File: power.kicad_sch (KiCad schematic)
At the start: 22 parts, among them J5 Power In, Q1 Q_NMOS_GDS, U5 UMW_HT7533-1_3.3V_High-In_LDO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

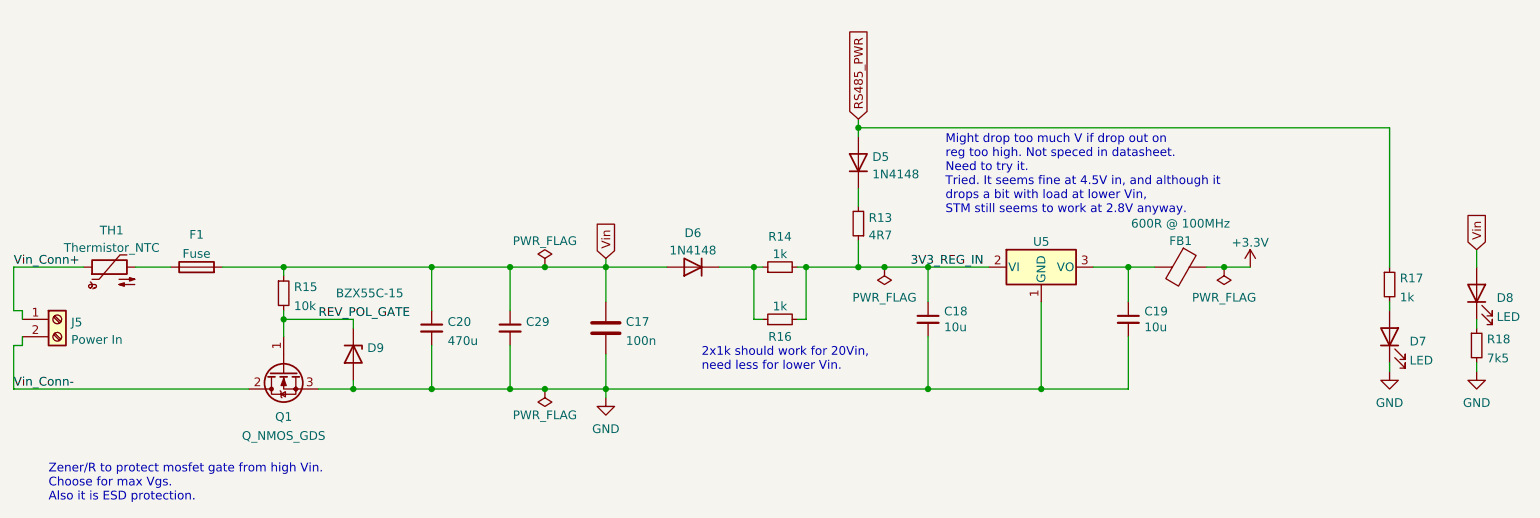
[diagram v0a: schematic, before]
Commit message: Schematic cleanup and readme improvement.
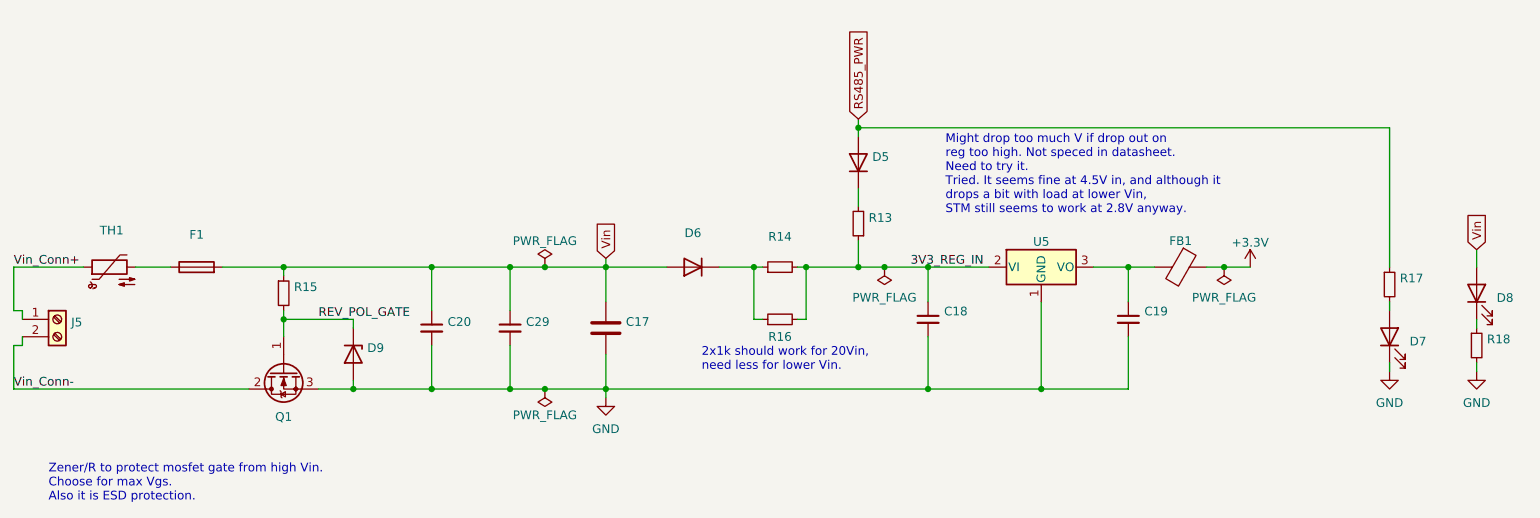
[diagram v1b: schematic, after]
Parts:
- C17: value 100n -> (none); footprint Capacitor_SMD:C_0805_2012Metric -> (none)
- C18, C19: value 10u -> (none); footprint Capacitor_SMD:C_0805_2012Metric -> (none)
- C20: value 470u -> (none); footprint Capacitor_THT:CP_Radial_D10.0mm_P5.00mm -> (none)
- C29: value ~ -> (none); footprint Capacitor_THT:CP_Radial_D10.0mm_P5.00mm -> (none)
- D5, D6: value 1N4148 -> (none); footprint Diode_THT:D_DO-35_SOD27_P7.62mm_Horizontal -> (none)
- D7, D8: value LED -> (none); footprint LED_SMD:LED_0805_2012Metric -> (none)
- D9: value BZX55C-15 -> (none); footprint Diode_THT:D_DO-35_SOD27_P7.62mm_Horizontal -> (none)
- F1: value Fuse -> (none); footprint Fuse:Fuseholder_Cylinder-5x20mm_Schurter_0031_8201_Horizontal_Open -> (none)
- FB1: value 600R @ 100MHz -> (none); footprint Inductor_SMD:L_0805_2012Metric -> (none)
- J5: value Power In -> (none); footprint river:TerminalBlock_KEFENG_Blue_2 -> (none)
- Q1: value Q_NMOS_GDS -> (none); footprint Package_TO_SOT_SMD:TO-252-3_TabPin2 -> (none)
- R13: value 4R7 -> (none); footprint Resistor_THT:R_Axial_DIN0309_L9.0mm_D3.2mm_P12.70mm_Horizontal -> (none)
- R14, R16: value 1k -> (none); footprint Resistor_THT:R_Axial_DIN0309_L9.0mm_D3.2mm_P12.70mm_Horizontal -> (none)
- R15: value 10k -> (none); footprint Resistor_SMD:R_0805_2012Metric_Pad1.20x1.40mm_HandSolder -> (none)
- R17: value 1k -> (none); footprint Resistor_SMD:R_0805_2012Metric -> (none)
- R18: value 7k5 -> (none); footprint Resistor_SMD:R_0805_2012Metric -> (none)
- TH1: value Thermistor_NTC -> (none); footprint Capacitor_THT:C_Disc_D7.5mm_W5.0mm_P7.50mm -> (none)
- U5: value UMW_HT7533-1_3.3V_High-In_LDO_SOT89 -> (none); footprint Package_TO_SOT_SMD:SOT-89-3 -> (none)
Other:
- company: (none) -> River Cat
- title: (none) -> Plant Light LED Driver
